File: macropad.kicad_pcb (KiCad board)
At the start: 2 copper layers, 78.5 x 59.5 mm, 47 parts, among them J1 DX07S016JA1R1500, SW1 SW_Push, SW10 SW_Push, SW2 SW_Push, SW3 SW_Push, SW5 SW_Push, SW6 SW_Push, SW7 SW_Push, SW8 SW_Push, SW9 SW_Push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

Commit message: Improvements
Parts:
- moved C3 18.8 mm to (145.7, 74.5)
- moved R12 16.5 mm to (145.7, 76.1)
- moved D3 8.52 mm to (149.0, 78.5), turned to 0 degrees
- moved D6 8.52 mm to (168.5, 78.5), turned to 0 degrees
- moved D9 8.51 mm to (188.0, 78.5), turned to 0 degrees
- moved D10 8.50 mm to (188.0, 98.0), turned to 0 degrees
- moved D1 8.50 mm to (129.5, 78.5), turned to 0 degrees
- moved D2 8.50 mm to (129.5, 98.0), turned to 0 degrees
- moved D4 8.50 mm to (149.0, 98.0), turned to 0 degrees
- moved D7 8.49 mm to (168.5, 98.0), turned to 0 degrees
- moved R7 7.32 mm to (155.3, 75.1)
- moved R5 5.25 mm to (158.4, 75.1)
- moved R4 3.71 mm to (158.4, 73.6)
- moved C6 3.42 mm to (152.2, 73.6), turned to 180 degrees
- moved C9 2.50 mm to (152.2, 75.1), turned to 180 degrees
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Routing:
- net /col3: track 44.1 -> 88.2 mm, vias 0 -> 1
- net /col2: track 67.7 -> 92.6 mm, vias 0 -> 1
- net /col0: track 19.5 -> 39.4 mm
- net Net-(MT1-PadB): track 0.00 -> 15.8 mm
- net /d+: track 0.04 -> 13.0 mm, vias 0 -> 2
- net Net-(MT1-PadA): track 0.00 -> 11.5 mm
- net /d-: track 0.00 -> 11.1 mm, vias 0 -> 2
- net /col1: track 19.5 -> 30.1 mm, vias 0 -> 1
- net /5V: track 7.83 -> 14.2 mm, vias 2 -> 6
- net GND: track 5.61 -> 9.05 mm
- net Net-(R12-Pad1): track 0.00 -> 2.36 mm
- net Net-(D10-Pad2): track 5.85 -> 3.61 mm
- net Net-(D9-Pad2): track 5.85 -> 3.63 mm
- net Net-(C3-Pad1): track 0.00 -> 1.69 mm
- net /rotary_1_b: track 0.00 -> 1.49 mm
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
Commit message: Fix everything forever
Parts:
- moved C2 14.7 mm to (145.7, 65.1)
- moved C1 11.5 mm to (145.7, 66.6)
- moved R3 4.38 mm to (137.0, 59.2), turned to 90 degrees
- moved G*** 1.42 mm to (126.1, 66.9)
- moved Y1 1.41 mm to (142.3, 66.7), turned to 90 degrees
- moved J1 0.84 mm to (153.7, 61.6)
- moved SW1 0.60 mm to (142.5, 60.4)
- moved R12 0.10 mm to (145.7, 76.0)
- moved C3 0.10 mm to (145.7, 74.4)
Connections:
- Y1 pad 2: Net-(C2-Pad1) -> GND
- Y1 pad 3: (no net) -> Net-(C2-Pad1)
- Y1 pad 4: (no net) -> GND
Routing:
- net /rotary_2_b: track 3.79 -> 51.8 mm, vias 0 -> 2
- net /rotary_2_a: track 3.15 -> 50.3 mm, vias 0 -> 2
- net /row2: track 59.9 -> 96.4 mm
- net /col2: track 92.6 -> 122.2 mm, vias 1 -> 4
- net Net-(R3-Pad2): track 0.00 -> 19.1 mm
- net /rotary_1_b: track 1.49 -> 20.3 mm, vias 0 -> 2
- net /rotary_1_a: track 1.48 -> 17.5 mm, vias 0 -> 2
- net Net-(C2-Pad1): track 0.00 -> 12.5 mm, vias 0 -> 2
- net /5V: track 14.2 -> 25.8 mm, vias 6 -> 10
- net /row1: track 59.9 -> 66.1 mm, vias 0 -> 2
- net Net-(J1-Pad5): track 0.00 -> 6.01 mm
- net GND: track 9.05 -> 14.9 mm
- net Net-(J1-Pad6): track 0.06 -> 3.39 mm

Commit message: Some aesthetic cleanup
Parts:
- moved G*** 0.63 mm to (125.9, 67.5)
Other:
- board size 78.5 x 59.5 mm -> 79.6 x 60.1 mm
- board text added: "Eric Wood 3/21"
- board text added: "PB0-2 -> row0-2 PB3-6 -> col0-3 pd0-1 -> rotary 1 pd2-3 -> rotary 2"
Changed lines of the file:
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@@
   (general
     (thickness 1.6)
-    (drawings 4)
+    (drawings 10)
     (tracks 299)
     (zones 0)
@@
   )
   (module dsp_dev_board:frankie (layer F.Cu)
-    (at 126.065 66.925)
+    (at 125.875 67.5282)
     (fp_text reference G*** (at 0 0) (layer F.SilkS) hide
       (effects (font (size 1.524 1.524) (thickness 0.3)))
@@
     )
   )
-  (gr_line (start 198 56.5) (end 198 116) (layer Edge.Cuts) (width 0.1))
-  (gr_line (start 119.5 56.5) (end 198 56.5) (layer Edge.Cuts) (width 0.1))
-  (gr_line (start 119.5 116) (end 119.5 56.5) (layer Edge.Cuts) (width 0.1))
-  (gr_line (start 198 116) (end 119.5 116) (layer Edge.Cuts) (width 0.1))
+  (gr_text "PB0-2 -> row0-2\nPB3-6 -> col0-3\npd0-1 -> rotary 1\npd2-3 -> rotary 2" (at 160.175 93.825 180) (layer B.SilkS)
+    (effects (font (size 1 1) (thickness 0.15)) (justify mirror))
+  )
+  (gr_text "Eric Wood 3/21" (at 120.875 88.475 90) (layer B.SilkS)
+    (effects (font (size 1.5 1.5) (thickness 0.3)) (justify mirror))
+  )
+  (gr_line (start 118.925 115.625) (end 118.925 59.525) (layer Edge.Cuts) (width 0.05))
+  (gr_arc (start 121.925 59.525) (end 121.925 56.525) (angle -90) (layer Edge.Cuts) (width 0.05))
+  (gr_arc (start 195.525 59.525) (end 198.525 59.525) (angle -90) (layer Edge.Cuts) (width 0.05))
+  (gr_arc (start 197.525 115.625) (end 197.525 116.625) (angle -90) (layer Edge.Cuts) (width 0.05))
+  (gr_arc (start 119.925 115.625) (end 118.925 115.625) (angle -90) (layer Edge.Cuts) (width 0.05))
+  (gr_line (start 195.525 56.525) (end 121.925 56.525) (layer Edge.Cuts) (width 0.05))
+  (gr_line (start 198.525 115.625) (end 198.525 59.525) (layer Edge.Cuts) (width 0.05))
+  (gr_line (start 119.925 116.625) (end 197.525 116.625) (layer Edge.Cuts) (width 0.05))
   (segment (start 140.92501 74.50001) (end 140.725 74.3) (width 0.25) (layer F.Cu) (net 1) (status 30))
   (segment (start 141.2875 73.475) (end 141.0375 73.225) (width 0.25) (layer F.Cu) (net 1) (status 30))
@@
     (polygon
       (pts
-        (xy 198 116) (xy 119.6 116) (xy 119.6 56.6) (xy 198 56.6)
+        (xy 198.525 116.525) (xy 119.025 116.525) (xy 119.025 56.525) (xy 198.525 56.525)
       )
     )
@@
     (polygon
       (pts
-        (xy 198 116) (xy 119.6 116) (xy 119.6 56.6) (xy 198 56.6)
+        (xy 198.525 116.525) (xy 119.025 116.525) (xy 119.025 56.525) (xy 198.525 56.525)
       )
     )

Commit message: Finalized layout
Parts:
- moved J1 1.00 mm to (153.7, 60.6)
- moved R1 1.00 mm to (152.3, 65.1)
- moved R2 1.00 mm to (154.0, 65.1)
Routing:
- net /d-: track 11.1 -> 12.1 mm
- net /d+: track 13.0 -> 13.5 mm
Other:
- board size 79.6 x 60.1 mm -> 79.6 x 61.1 mm

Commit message: copper frankie
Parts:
- removed the G*** at (125.9, 67.5)
- added G***: LOGO, dsp_dev_board:frankie_solder_mask, F.Cu at (127.0, 66.8)
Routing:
- added copper zone on F.Cu, net (none)

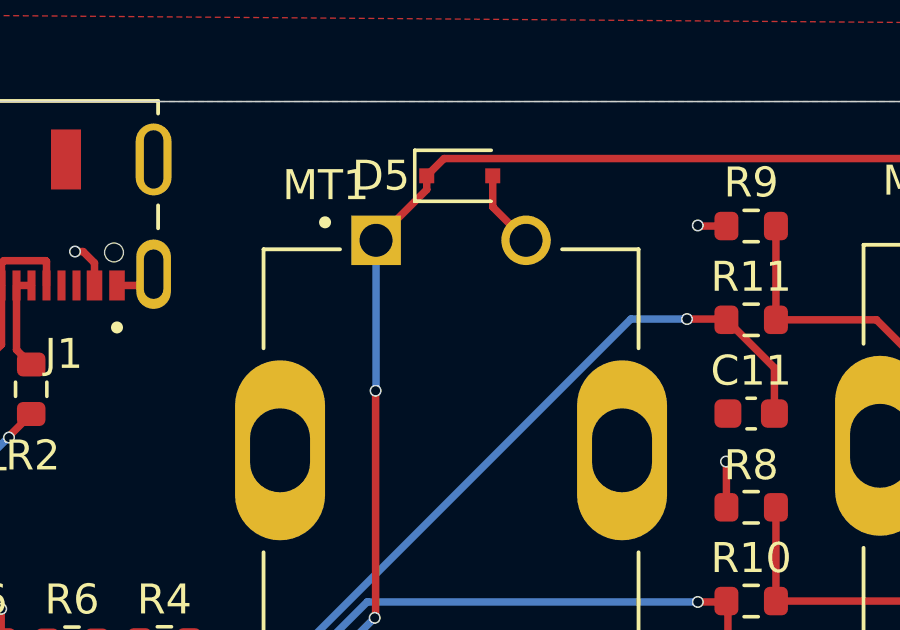
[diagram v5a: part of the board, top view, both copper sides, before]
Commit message: Add JLC to silkscreen
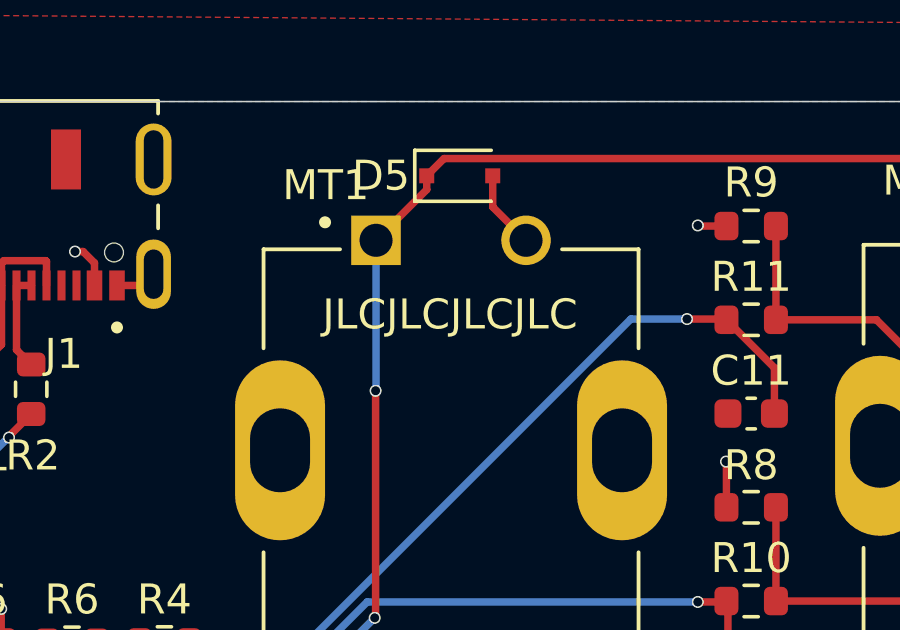
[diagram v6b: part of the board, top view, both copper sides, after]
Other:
- board text added: "JLCJLCJLCJLC"

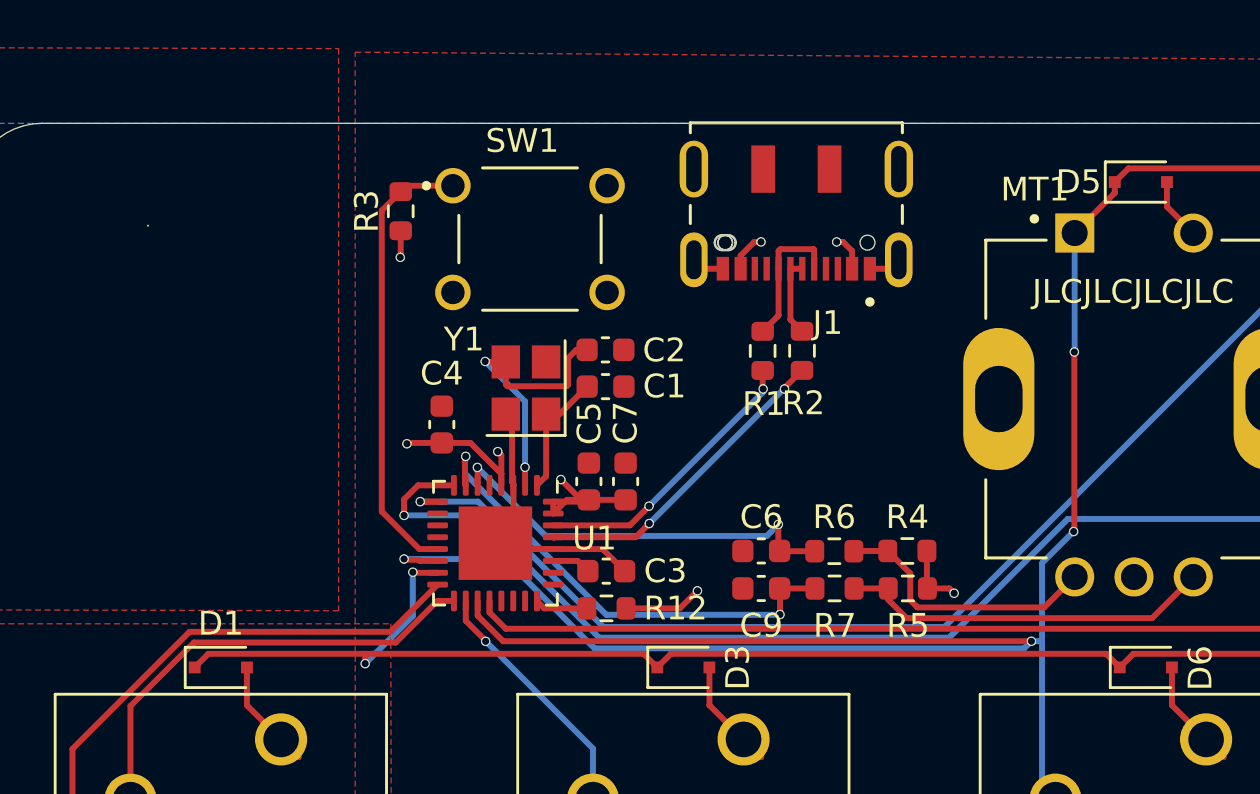
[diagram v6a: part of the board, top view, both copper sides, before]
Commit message: Fix bugs discovered in first board
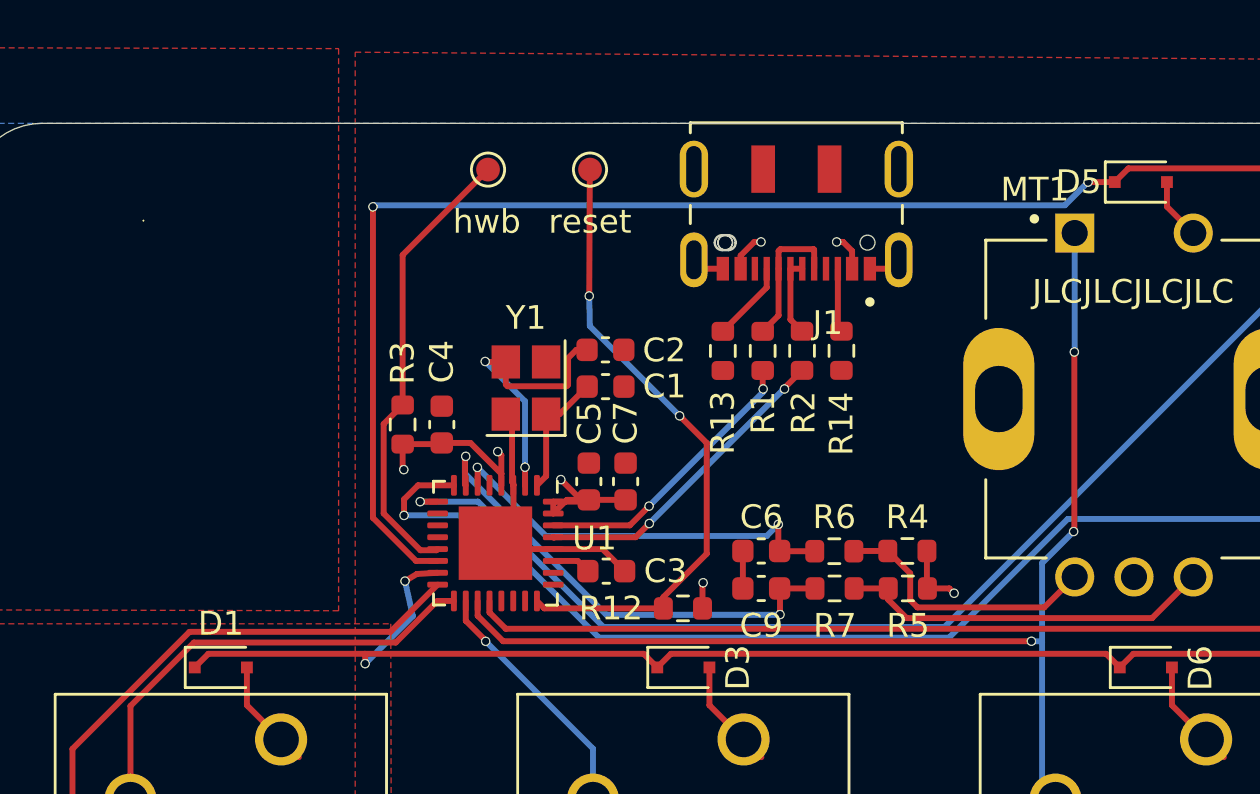
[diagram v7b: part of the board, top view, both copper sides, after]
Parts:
- removed SW1: SW_Push, 1825910-7:SW_1825910-7
- added R13: 5.1k, Resistor_SMD:R_0603_1608Metric, F.Cu at (150.6, 65.1)
- added R14: 5.1k, Resistor_SMD:R_0603_1608Metric, F.Cu at (155.6, 65.1)
- added hwb: ~HWB, TestPoint:TestPoint_Pad_D1.0mm, F.Cu at (140.7, 57.5)
- added reset: ~RESET, TestPoint:TestPoint_Pad_D1.0mm, F.Cu at (145.0, 57.5)
- moved R3 9.00 mm to (137.1, 68.2)
- moved R12 3.22 mm to (148.9, 76.0)
- moved G*** 0.29 mm to (126.8, 66.6)
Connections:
- D5 pad 1: /col2 -> /row0
- D8 pad 1: /col2 -> /row0
- U1 pad 14: /col2 -> /row0
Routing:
- net /row0: track 0.00 -> 69.0 mm, vias 0 -> 2
- net /col2: track 122.2 -> 69.2 mm, vias 4 -> 3
- net Net-(R12-Pad1): track 2.30 -> 26.8 mm, vias 0 -> 2
- net Net-(J1-Pad9): track 0.00 -> 3.41 mm
- net Net-(J1-Pad3): track 0.00 -> 2.70 mm
- net /5V: track 25.8 -> 23.7 mm, vias 10 -> 9
- net GND: track 14.9 -> 16.5 mm

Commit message: Add v2 and plot gerbers
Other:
- board text added: "v2"
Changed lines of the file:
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@@
   (general
     (thickness 1.6)
-    (drawings 11)
+    (drawings 12)
     (tracks 314)
     (zones 0)
@@
     )
   )
+  (gr_text v2 (at 120.9896 100.4212 90) (layer B.SilkS)
+    (effects (font (size 1.5 1.5) (thickness 0.3)) (justify mirror))
+  )
   (gr_text JLCJLCJLCJLC (at 167.925 62.625) (layer F.SilkS)
